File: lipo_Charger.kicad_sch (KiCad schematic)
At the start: 0 parts

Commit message: progress 1
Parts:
- added C1, C2: 47nf, symbol Device:C
- added C10, C9: 0.033uf, symbol Device:C
- added C11: 0.1uf, symbol Device:C
- added C12, C5, C6, C7, C8: 10uf, symbol Device:C
- added C3: 3.3uf, symbol Device:C
- added C4: 1uf, symbol Device:C
- added L1: L, symbol Device:L
- added R1, R2: R, symbol Device:R
- added R10: 0.01ohm, symbol Device:R
- added R11, R12: 10ohm, symbol Device:R
- added R13, R3, R4, R5, R6: 10K, symbol Device:R
- added R7: 10mohm, symbol Device:R
- added R8, R9: 4.99ohm, symbol Device:R
- added U1: BQ25703ARSNR, Lipo_Charger_footprint:RSN0032B(1), symbol Lipo_charger_sym:BQ25703ARSNR
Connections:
- new net: R1.2, R2.1, U1.18 (CELL_BATPRES)
- new net: R12.1, U1.19 (SRN)
- new net: C10.1, R9.1, U1.2 (ACN)
- new net: R11.1, U1.20 (SRP)
- new net: C2.2, U1.25 (BTST2)
- new net: C3.1, U1.28 (REGN)
- new net: C9.1, R8.1, U1.3 (ACP)
- new net: C1.2, U1.30 (BTST1)
- new net: C11.1, R10.1, R11.2
- new net: R7.1, R8.2
- new net: R7.2, R9.2
- new net: C1.1, L1.1
- new net: C2.1, L1.2
- new net +24V: C4.1, C5.1, C6.1, C7.1, C8.1
- new net BAT: C11.2, C12.1, R10.2, R12.2
- new net CHRG_OK: R5.2, U1.4 (CHRG_OK)
- new net CMPOUT: R13.2, U1.15 (CMPOUT)
- new net EN_OTG: R6.2, U1.5 (EN_OTG)
- new net GND: C10.2, C12.2, C3.2, C9.2, R2.2, U1.27 (PGND), U1.33 (PAD)
- new net SCL: R4.2, U1.12 (SDA)
- new net SDA: R3.2, U1.13 (SCL)
- new net VDDA: R1.1, R13.1, R3.1, R4.1, R5.1, R6.1
- no-connect marks 0 -> 1

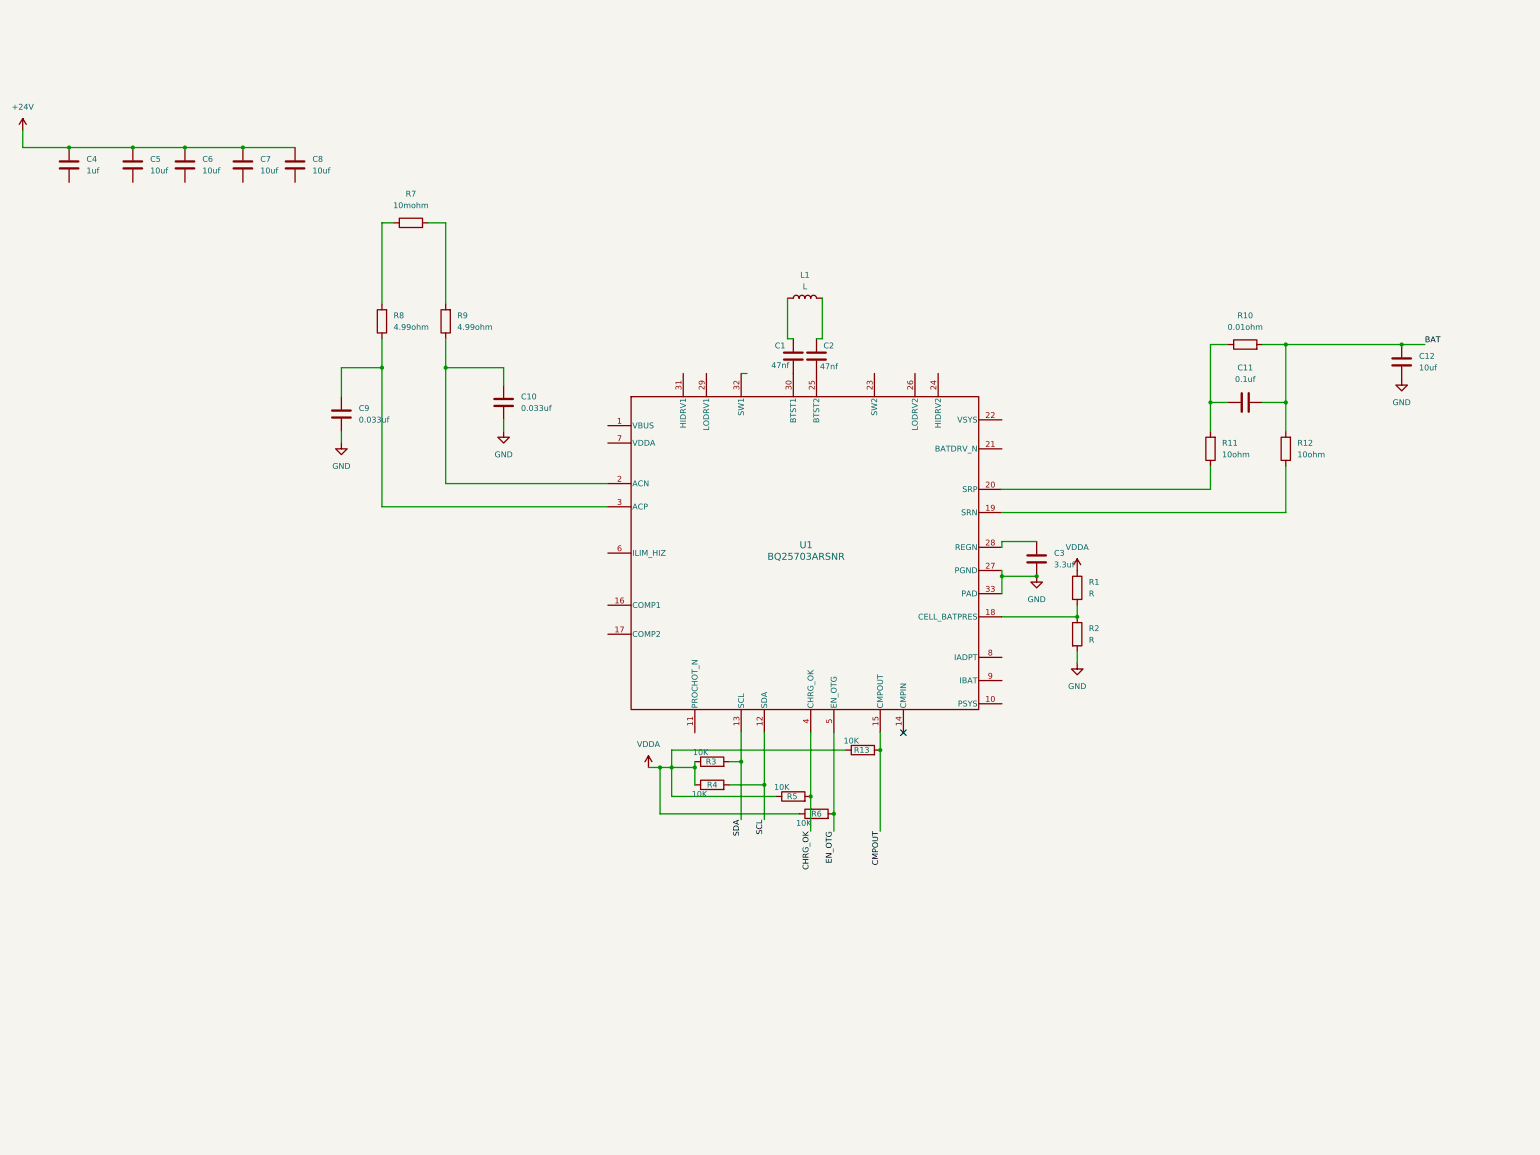
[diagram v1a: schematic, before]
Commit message: progress overall sch for the ti ic has done now need to get the actual comp and then update it
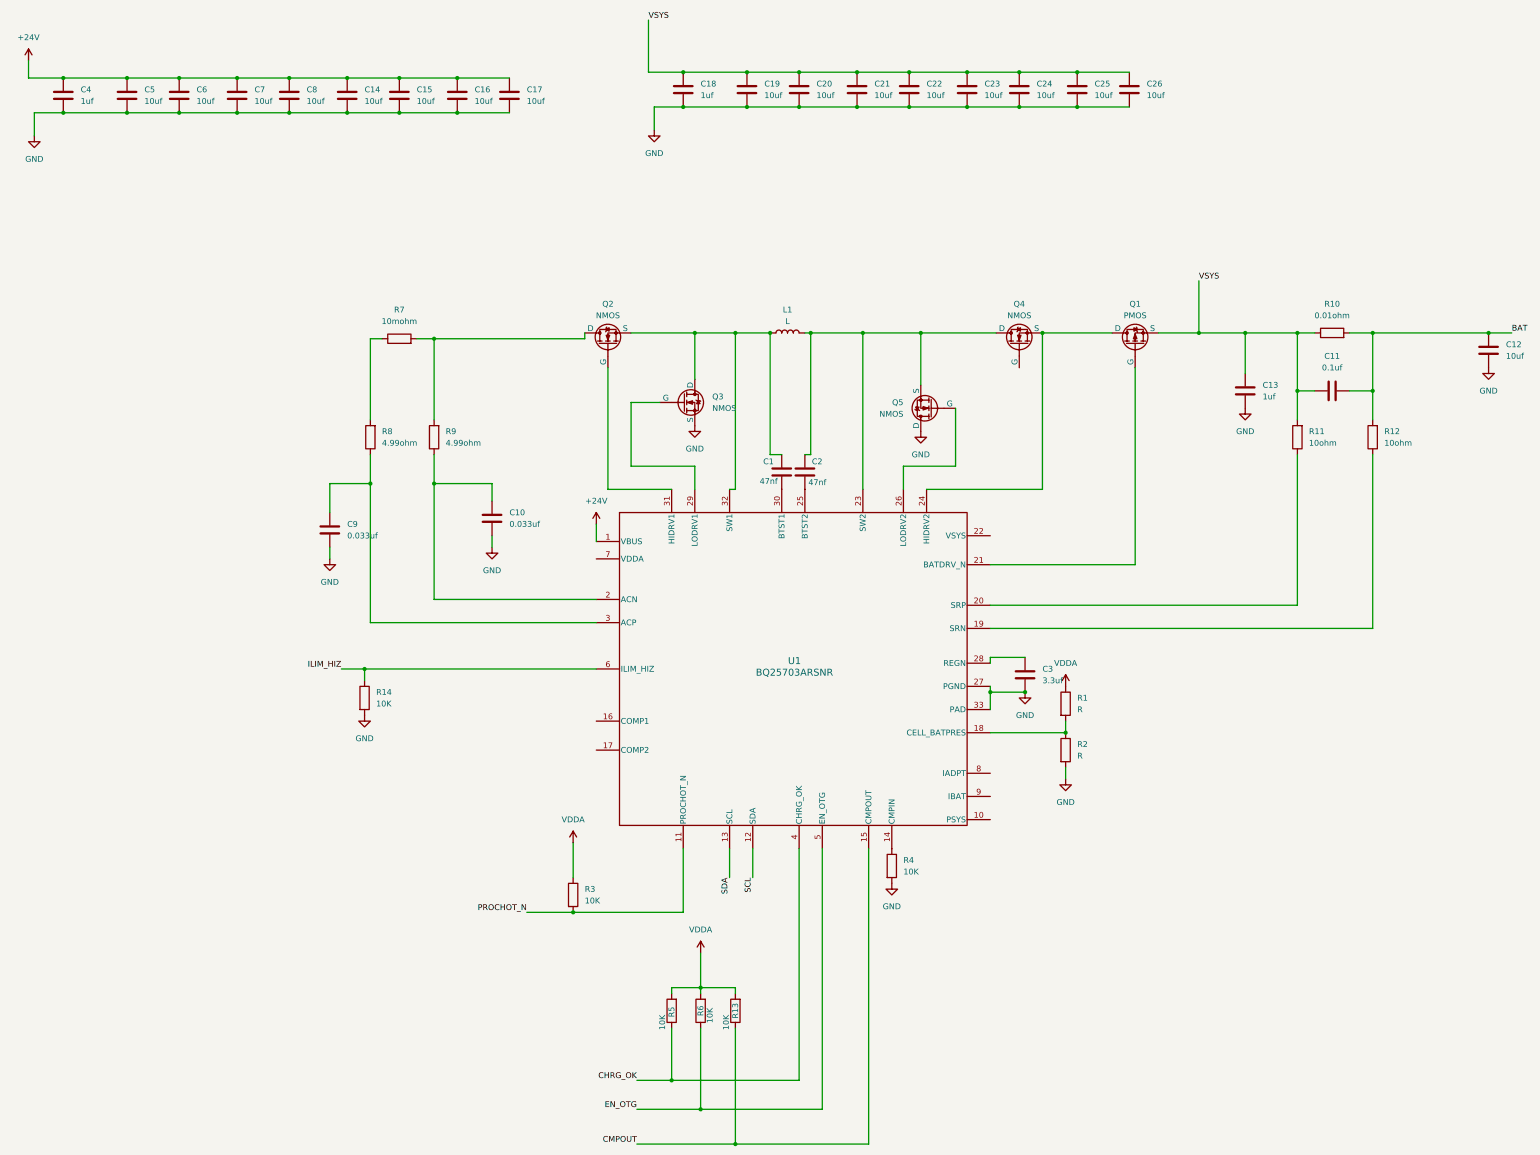
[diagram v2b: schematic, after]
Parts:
- added C13, C18: 1uf, symbol Device:C
- added C14, C15, C16, C17, C19, C20, C21, C22, C23, C24, C25, C26: 10uf, symbol Device:C
- added Q1: PMOS, symbol Simulation_SPICE:PMOS
- added Q2, Q3, Q4, Q5: NMOS, symbol Simulation_SPICE:NMOS
- added R14: 10K, symbol Device:R
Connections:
- net +24V: now also U1.1 (VBUS), C14.1, C15.1, C16.1, C17.1
- net CHRG_OK: now also R5.1; no longer R5.2
- net CMPOUT: now also R13.1; no longer R13.2
- net EN_OTG: now also R6.1; no longer R6.2
- net GND: now also C4.2, C5.2, C6.2, C7.2, C8.2, R4.2, C13.1, C14.2, C15.2, C16.2, C17.2, C18.2, C19.2, C20.2, C21.2, C22.2, C23.2, C24.2, C25.2, C26.2, Q3.3 (S), Q5.1 (D), R14.2
- net SCL: no longer R4.2
- net SDA: no longer R3.2
- net VDDA: now also R13.2, R5.2, R6.2; no longer R13.1, R4.1, R5.1, R6.1
- net PROCHOT_N: now reaches U1.11 (PROCHOT_N)
- net PROCHOT_N: now also R3.2
- net at U1.14 (CMPIN): now also R4.1
- net at U1.21 (BATDRV_N): now also Q1.2 (G)
- net at U1.23 (SW2): now also C2.1, L1.2, Q4.1 (D), Q5.3 (S)
- net at U1.24 (HIDRV2): now also Q1.1 (D), Q4.3 (S)
- net at U1.26 (LODRV2): now also Q5.2 (G)
- net at U1.29 (LODRV1): now also Q3.2 (G)
- net at U1.31 (HIDRV1): now also Q2.2 (G)
- net at U1.32 (SW1): now also C1.1, L1.1, Q2.3 (S), Q3.1 (D)
- net ILIM_HIZ: now reaches U1.6 (ILIM_HIZ)
- net ILIM_HIZ: now also R14.1
- net VSYS: now reaches C11.1, R10.1, R11.2
- net VSYS: now also C13.2, C18.1, C19.1, C20.1, C21.1, C22.1, C23.1, C24.1, C25.1, C26.1, Q1.3 (S)
- net at R7.2, R9.2: now also Q2.1 (D)
- no-connect marks 1 -> 0
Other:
- moved on the sheet: C1, C10, C11, C12, C2, C3, C4, C5, C6, C7, C8, C9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

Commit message: some changes made
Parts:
- L1: value L -> 2.2uh
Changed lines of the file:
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@@
 			)
 		)
-		(property "Value" "L"
+		(property "Value" "2.2uh"
 			(at 187.96 87.63 90)
 			(effects

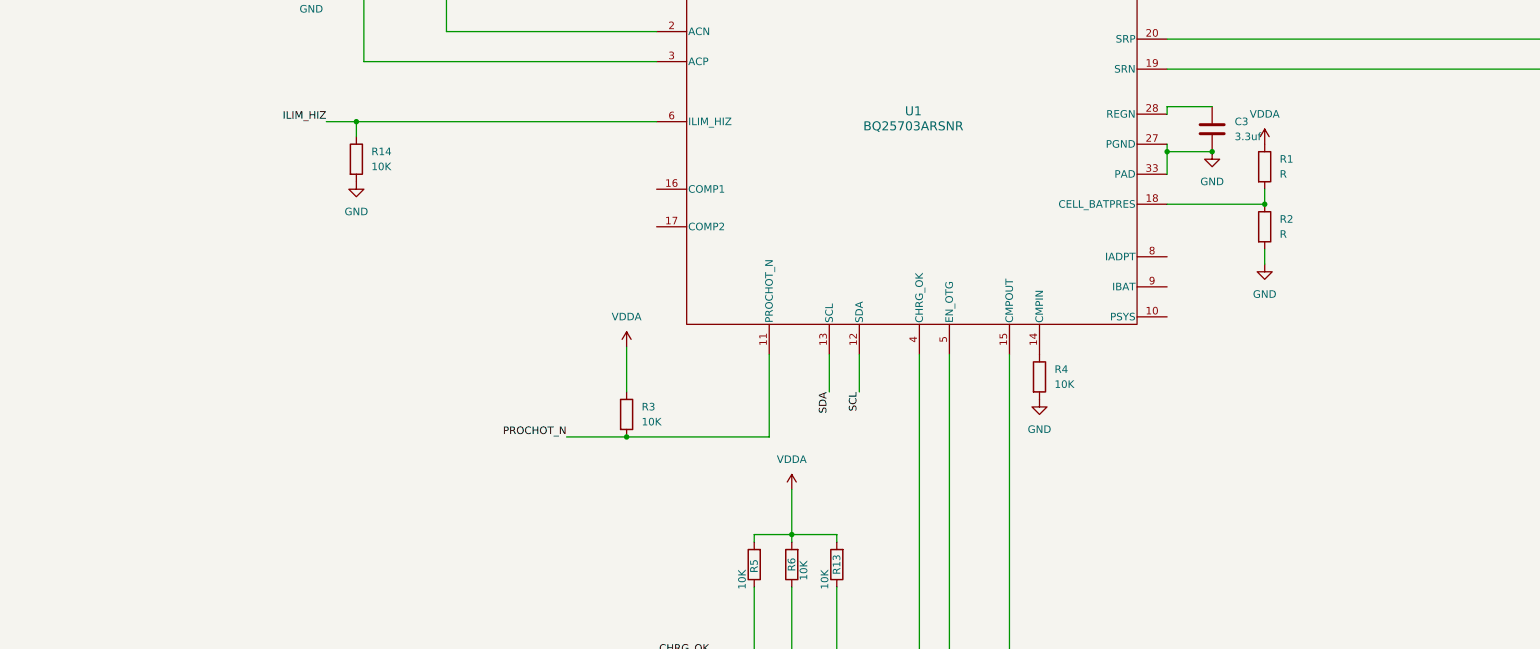
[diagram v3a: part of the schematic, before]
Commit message: current sensing pins have connected the req components
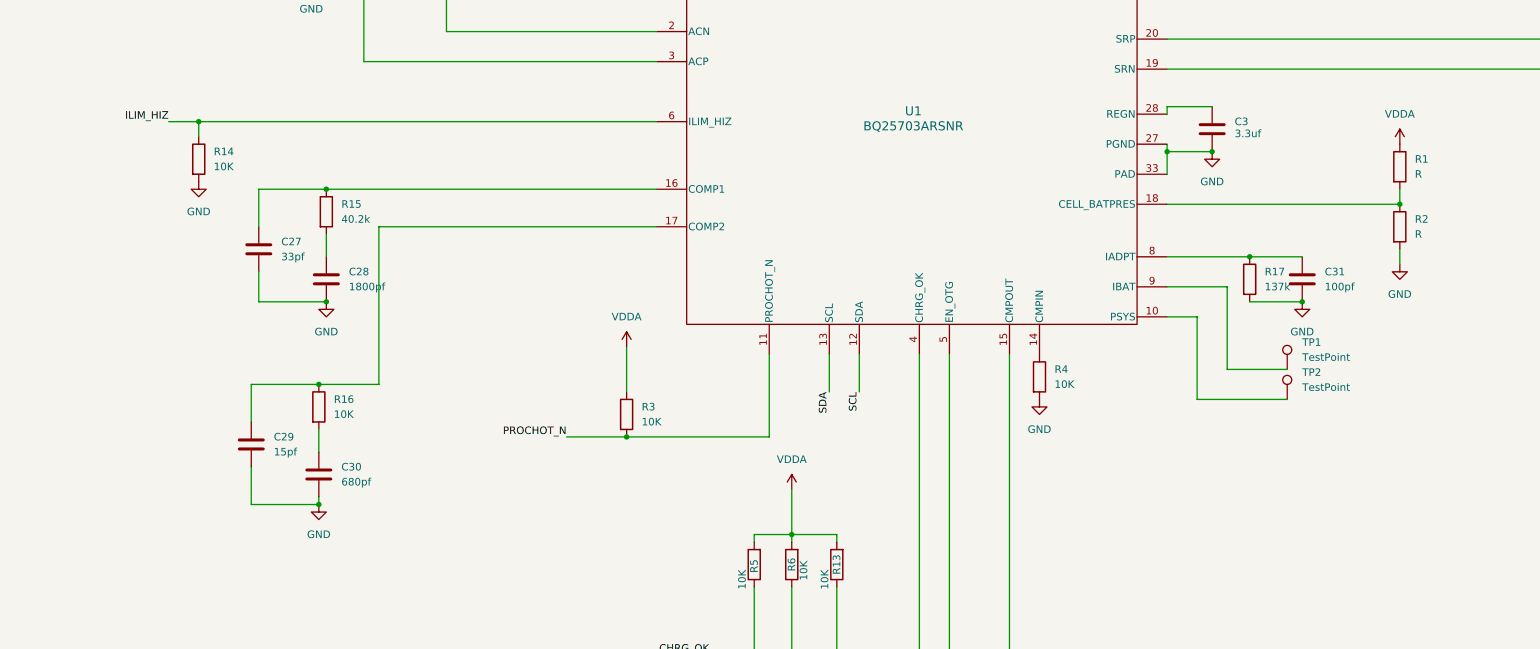
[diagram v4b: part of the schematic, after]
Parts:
- added C27: 33pf, symbol Device:C
- added C28: 1800pf, symbol Device:C
- added C29: 15pf, symbol Device:C
- added C30: 680pf, symbol Device:C
- added C31: 100pf, symbol Device:C
- added R15: 40.2k, symbol Device:R
- added R16: 10K, symbol Device:R
- added R17: 137k, symbol Device:R
- added TP1, TP2: TestPoint, symbol Connector:TestPoint
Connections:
- net GND: now also C27.2, C28.2, C29.2, C30.2, C31.2, R17.2
- net at U1.10 (PSYS): now also TP2.1
- net at U1.16 (COMP1): now also C27.1, R15.1
- net at U1.17 (COMP2): now also C29.1, R16.1
- net at U1.8 (IADPT): now also C31.1, R17.1
- net at U1.9 (IBAT): now also TP1.1
- new net: C28.1, R15.2
- new net: C30.1, R16.2
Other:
- moved on the sheet: R1, R14, R2

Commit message: bom generated need to assign footprints and review the sch add balancing and mcu circuit
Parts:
- U1: link (none) -> https://robu.in/product/cdrh104r-2-2%ce%bch-power-inductor-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
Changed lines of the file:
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@@
+			)
+		)
+		(property "link" "https://robu.in/product/cdrh104r-2-2%ce%bch-power-inductor-pack-of-5/#tab-specification"
+			(at 190.5 165.1 0)
+			(effects
+				(font
+					(size 1.27 1.27)
+				)
+				(hide yes)
 			)
 		)
